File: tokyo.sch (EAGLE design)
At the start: 50 parts, among them J1 254-2X5F, J2 254-2X5M, P1 9774050151, P2 9774050151, P3 9774050151, P4 9774050151, Q1 STD6N95K5, T1 750313823, U1 UCC28710, X1 508-1X3B

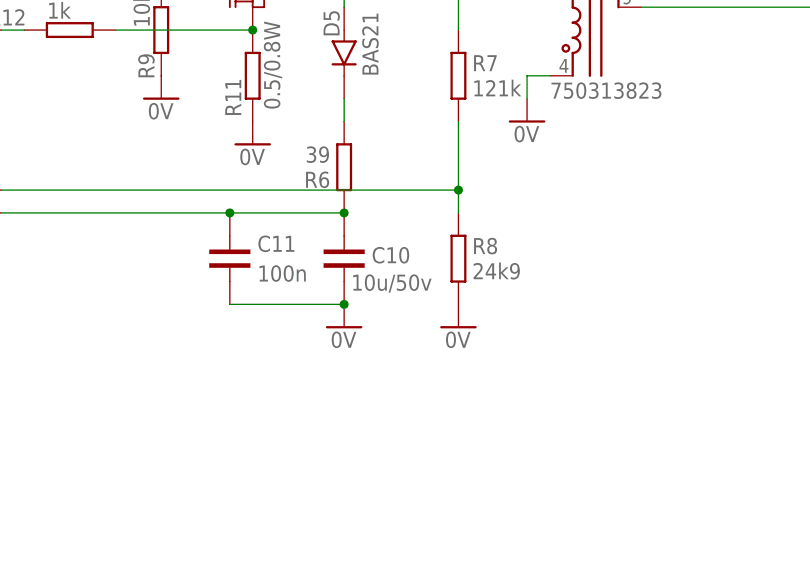
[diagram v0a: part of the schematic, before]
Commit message: Corrected value for C10.
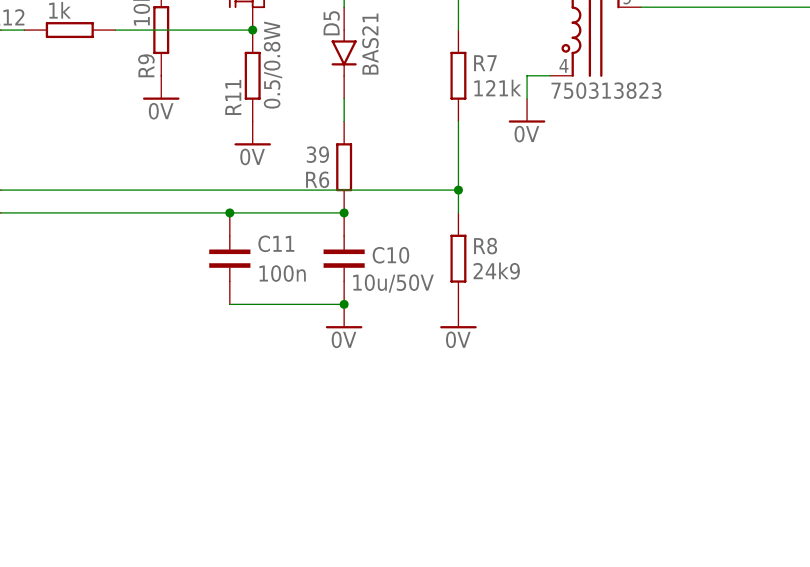
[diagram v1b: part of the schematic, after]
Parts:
- C10: value 10u/50v -> 10u/50V
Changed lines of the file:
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@@
 <part name="U1" library="integratedcircuits" deviceset="UCC28710" device=""/>
 <part name="D5" library="diodes" deviceset="BAS21" device=""/>
-<part name="C10" library="capacitors" deviceset="C" device="1206" value="10u/50v"/>
+<part name="C10" library="capacitors" deviceset="C" device="1206" value="10u/50V"/>
 <part name="R7" library="resistors" deviceset="R" device="0603" value="121k"/>
 <part name="R8" library="resistors" deviceset="R" device="0603" value="24k9"/>

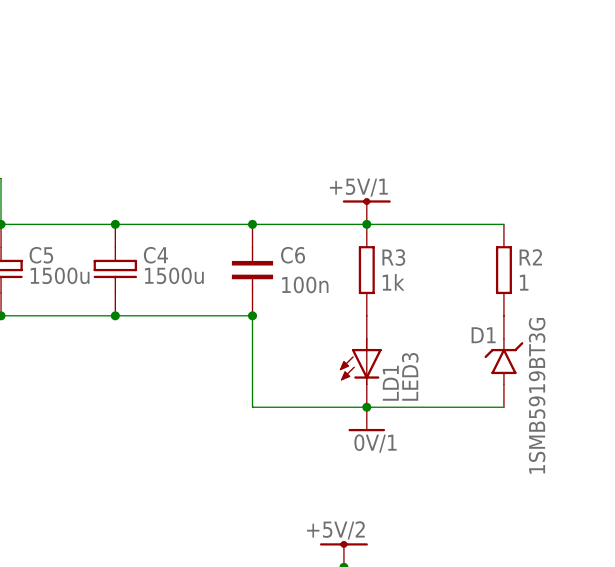
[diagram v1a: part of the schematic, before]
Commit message: Changed R3 to 330 (LD1 was too dim). Corrected BOM (LD1 should be a green LED).
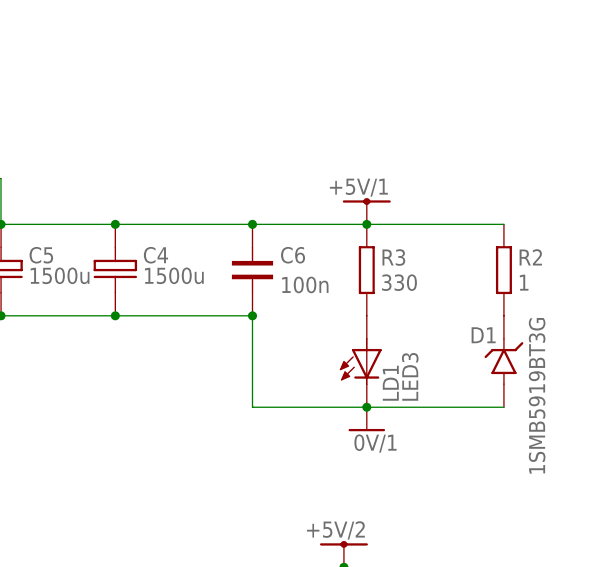
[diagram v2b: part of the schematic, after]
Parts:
- R3: value 1k -> 330
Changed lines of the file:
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@@
 <?xml version="1.0" encoding="utf-8"?>
 <!DOCTYPE eagle SYSTEM "eagle.dtd">
-<eagle version="7.2.0">
+<eagle version="7.3.0">
 <drawing>
 <settings>
@@
 <part name="R11" library="resistors" deviceset="R" device="2512" value="0.5/0.8W"/>
 <part name="C6" library="capacitors" deviceset="C" device="0603" value="100n"/>
-<part name="R3" library="resistors" deviceset="R" device="0603" value="1k"/>
+<part name="R3" library="resistors" deviceset="R" device="0603" value="330"/>
 <part name="R4" library="resistors" deviceset="R" device="1206" value="39"/>
 <part name="LD1" library="unsorted" deviceset="LED3" device=""/>

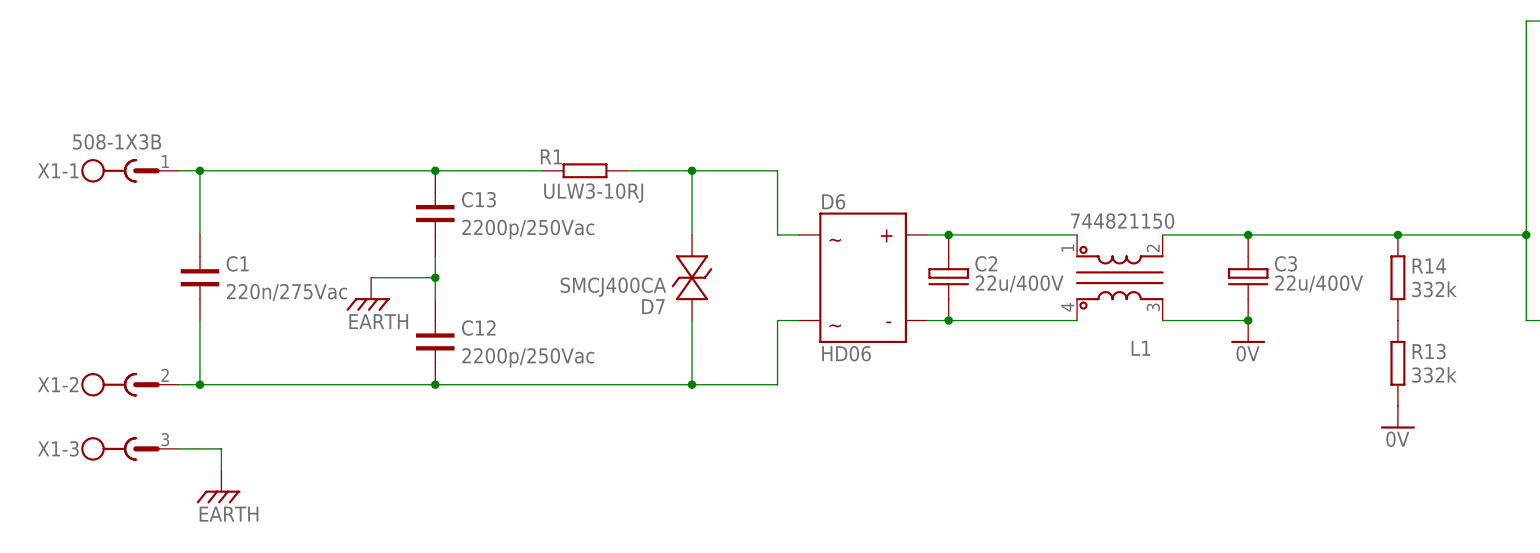
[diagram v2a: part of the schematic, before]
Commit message: Incorporated changes required for EMC tests: replaced transzorb with varistor, changed position of line choke.
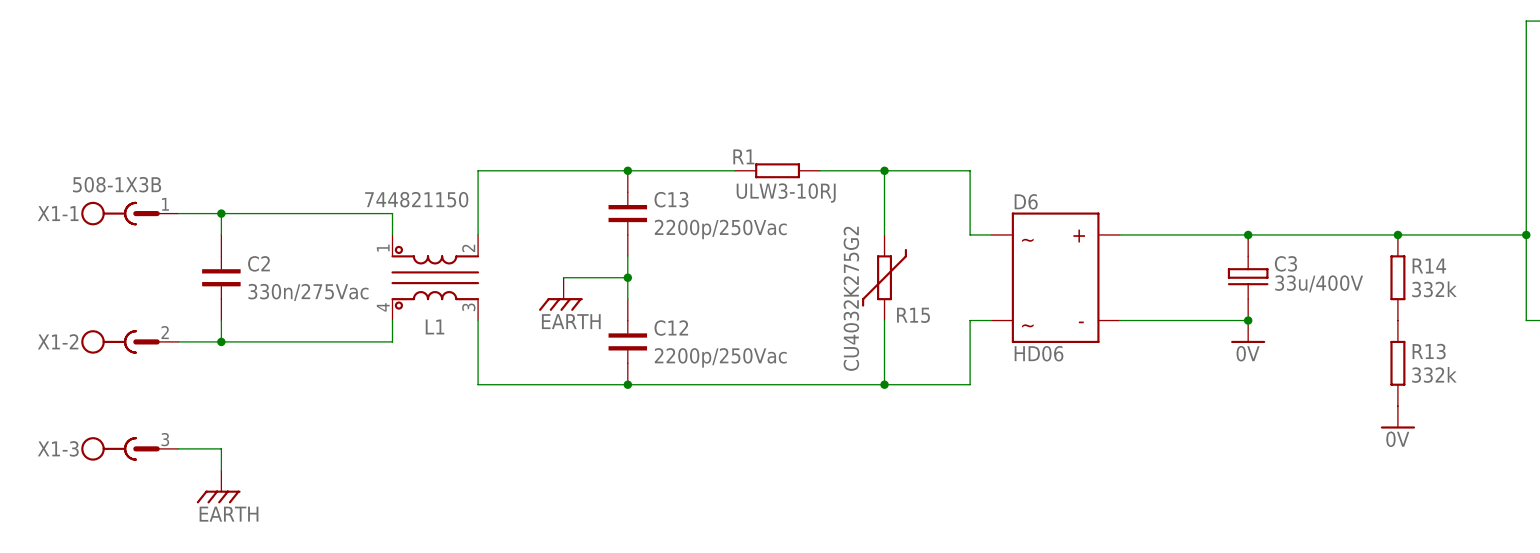
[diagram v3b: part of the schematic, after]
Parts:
- removed C1: 220n/275Vac, capacitors:C14X8
- removed D7: SMCJ400CA, supressors:SMCJ400CA
- added R15: CU4032K275G2, supressors:CU4032K275G2
- C2: value 22u/400V -> 330n/275Vac; device capacitors:C+D13 -> capacitors:C15X8.5
- C3: value 22u/400V -> 33u/400V; device capacitors:C+D13 -> capacitors:C+D18
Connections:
- removed net N$20: C2.2, D6.2, L1.4
- removed net N$21: C2.1, D6.1, L1.1
- new net N$19: C2.1, L1.1, X1-1.1
- new net N$22: C2.2, L1.4, X1-2.1
- net 0V: now also D6.2; no longer L1.3
- net N$1: now also L1.2; no longer C1.1, X1-1.1
- net N$2: now also L1.3, R15.2; no longer C1.2, D7.P$1, X1-2.1
- net N$4: now also R15.1; no longer D7.P$2
- net N$9: now also D6.1; no longer L1.2
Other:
- moved on the sheet: C12, C13, D6, L1, R1, X1-1, X1-2

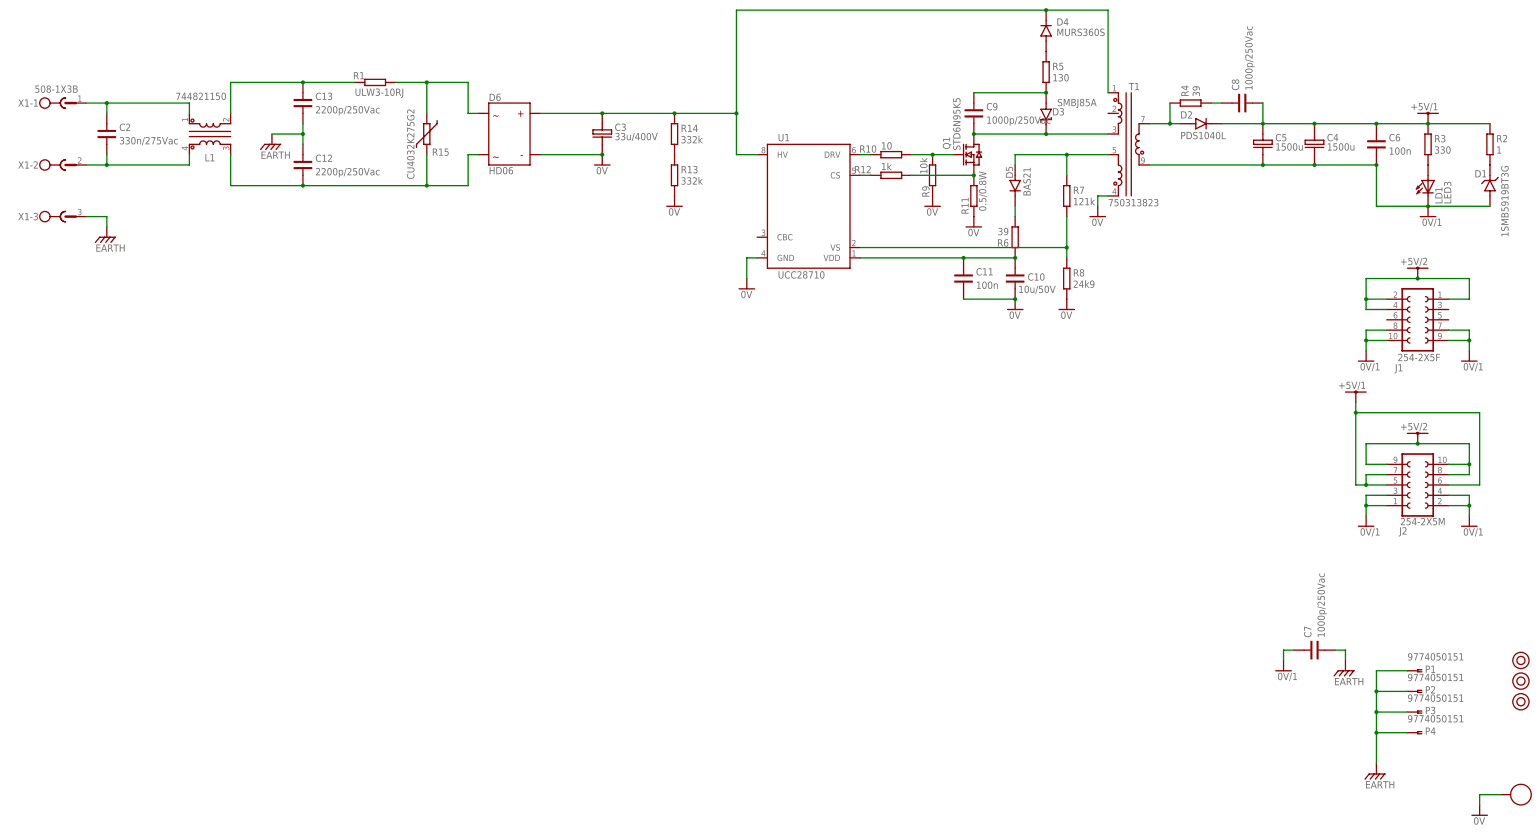
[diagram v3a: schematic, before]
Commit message: Changed R15 to 10 k due to bright LED usage. Renumbered all components.
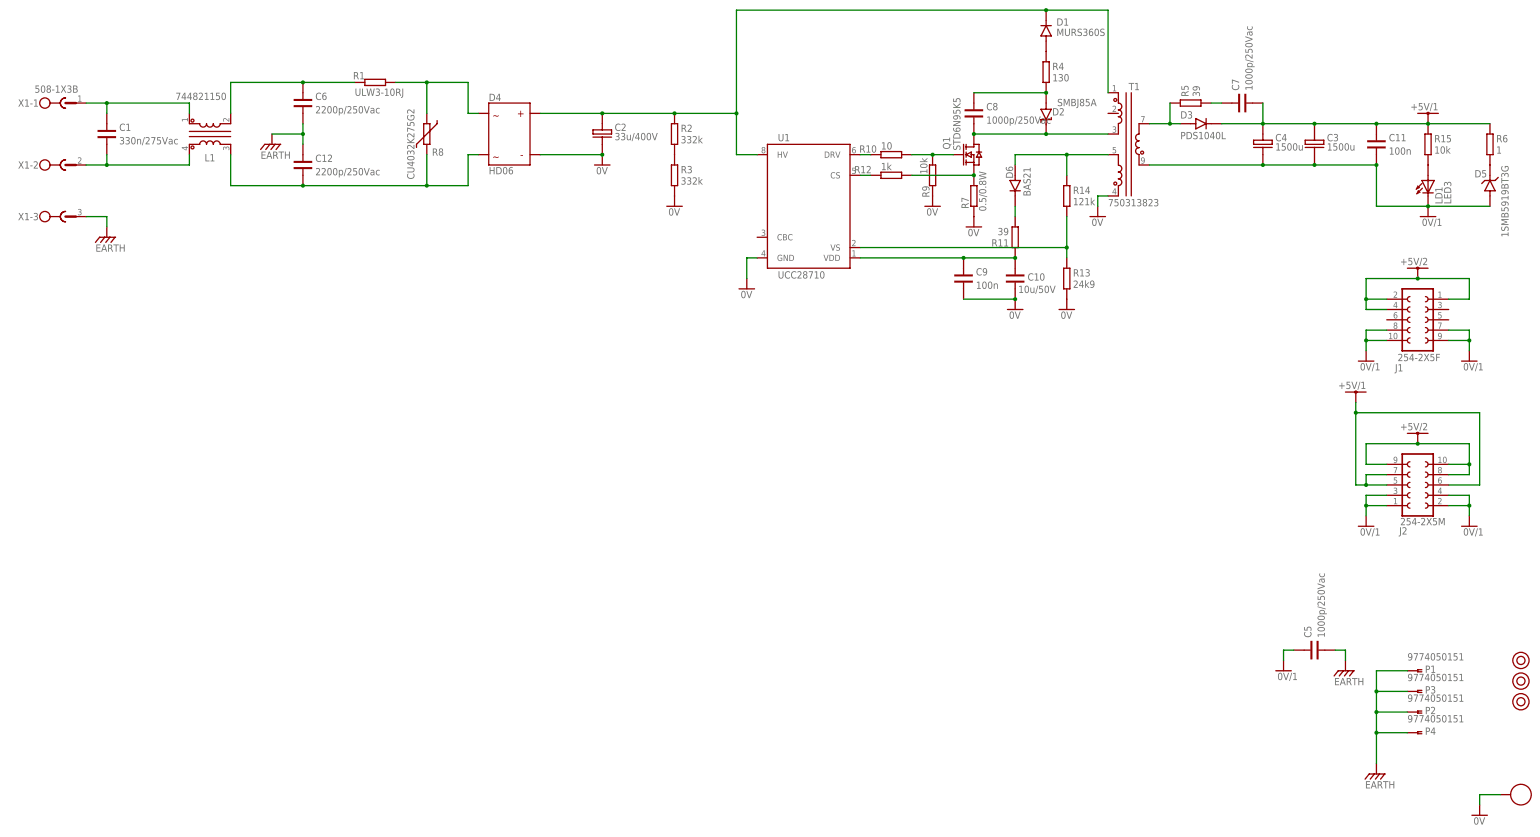
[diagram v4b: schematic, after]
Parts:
- removed C13: 2200p/250Vac, capacitors:C2211
- added C1: 330n/275Vac, capacitors:C15X8.5
- C2: value 330n/275Vac -> 33u/400V; device capacitors:C15X8.5 -> capacitors:C+D18
- C3: value 33u/400V -> 1500u; device capacitors:C+D18 -> capacitors:C+D10
- C5: value 1500u -> 1000p/250Vac; device capacitors:C+D10 -> capacitors:C1812
- C6: value 100n -> 2200p/250Vac; device capacitors:C0603 -> capacitors:C2211
- C9: value 1000p/250Vac -> 100n; device capacitors:C1812 -> capacitors:C0603
- D1: value 1SMB5919BT3G -> MURS360S; device diodes:1SMB5919BT3G -> diodes:MURS360S
- D2: value PDS1040L -> SMBJ85A; device diodes:PDS1040L -> supressors:SMBJ85A
- D3: value SMBJ85A -> PDS1040L; device supressors:SMBJ85A -> diodes:PDS1040L
- D4: value MURS360S -> HD06; device diodes:MURS360S -> diodes:HD06
- D5: value BAS21 -> 1SMB5919BT3G; device diodes:BAS21 -> diodes:1SMB5919BT3G
- D6: value HD06 -> BAS21; device diodes:HD06 -> diodes:BAS21
- R11: value 0.5/0.8W -> 39; device resistors:R2512 -> resistors:R0603
- R13: value 332k -> 24k9; device resistors:R1206 -> resistors:R0603
- R14: value 332k -> 121k; device resistors:R1206 -> resistors:R0603
- R15: value CU4032K275G2 -> 10k; device supressors:CU4032K275G2 -> resistors:R0603
- R2: value 1 -> 332k
- R3: value 330 -> 332k; device resistors:R0603 -> resistors:R1206
- R4: value 39 -> 130
- R5: value 130 -> 39
- R6: value 39 -> 1; device resistors:R0603 -> resistors:R1206
- R7: value 121k -> 0.5/0.8W; device resistors:R0603 -> resistors:R2512
- R8: value 24k9 -> CU4032K275G2; device resistors:R0603 -> supressors:CU4032K275G2
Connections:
- removed net N$16 (its old number): D1.1, R2.2
- new net N$26: D6.1, R11.2
- net +5V/1: now also C11.1, C3.1, C7.2, D3.1, R15.1, R6.1; no longer C5.1, C6.1, C8.2, D2.1, R2.1, R3.1
- net 0V: now also C2.2, C9.2, D4.2, R3.2, R7.1; no longer C11.2, C3.2, D6.2, R11.1, R8.2
- net 0V/1: now also C11.2, C3.2, C5.1, D5.2; no longer C5.2, C6.2, C7.1, D1.2
- net EARTH: now also C5.2, C6.2; no longer C13.2, C7.2
- net N$1: now also C6.1; no longer C13.1
- net N$10: now also D1.2, R4.1; no longer D4.2, R5.1
- net N$11: now also C8.2, D2.C; no longer C9.2, D3.C
- net N$12: now also R7.2; no longer R11.2
- net N$15: now also C9.1, R11.1; no longer C11.1, R6.1
- net N$17: now also C8.1, D2.A, R4.2; no longer C9.1, D3.A, R5.2
- net N$18: now also R13.1, R14.2; no longer R7.2, R8.1
- net N$19: now also C1.1; no longer C2.1
- net N$2: now also D4.4, R8.2; no longer D6.4, R15.2
- net N$22: now also C1.2; no longer C2.2
- net N$3: now also D6.2, R14.1; no longer D5.2, R7.1
- net N$4: now also D4.3, R8.1; no longer D6.3, R15.1
- net N$5: now also R15.2; no longer R3.2
- net N$6: now also C7.1, R5.2; no longer C8.1, R4.2
- net N$7: now also R2.2, R3.1; no longer R13.1, R14.2
- net N$8: now also D3.2, R5.1; no longer D2.2, R4.1
- net N$9: now also C2.1, D1.1, R2.1; no longer C3.1, D6.1, R14.1
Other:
- moved on the sheet: C11, C3, C4, C6, C7, C8, C9, P2, P3, R11, R13, R14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

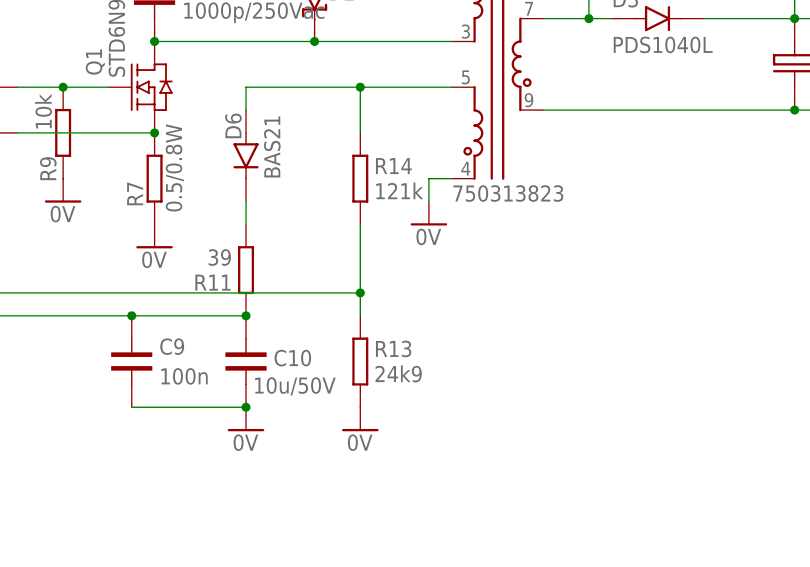
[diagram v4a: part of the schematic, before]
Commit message: Changed values of R13 and R14 in order to get +5.5V on output.
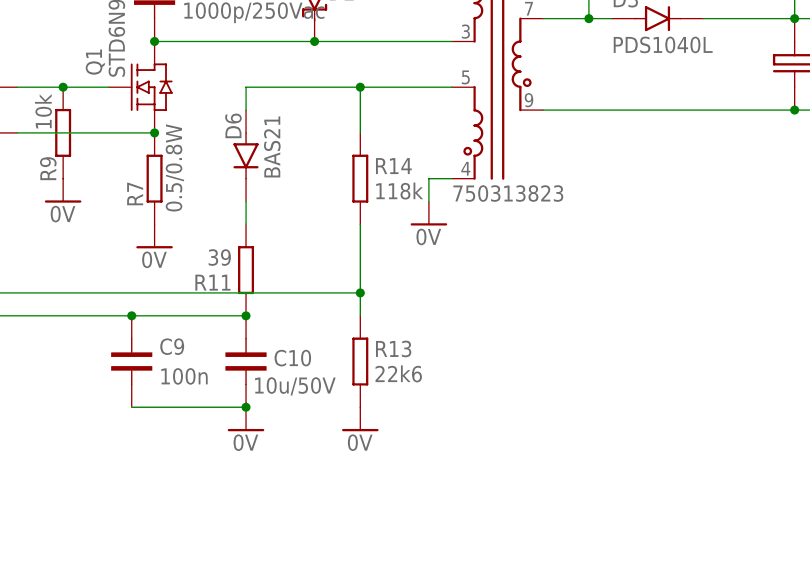
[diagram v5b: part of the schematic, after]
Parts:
- R13: value 24k9 -> 22k6
- R14: value 121k -> 118k
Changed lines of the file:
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@@
 <part name="D6" library="diodes" deviceset="BAS21" device=""/>
 <part name="C10" library="capacitors" deviceset="C" device="1206" value="10u/50V"/>
-<part name="R14" library="resistors" deviceset="R" device="0603" value="121k"/>
-<part name="R13" library="resistors" deviceset="R" device="0603" value="24k9"/>
+<part name="R14" library="resistors" deviceset="R" device="0603" value="118k"/>
+<part name="R13" library="resistors" deviceset="R" device="0603" value="22k6"/>
 <part name="R12" library="resistors" deviceset="R" device="0603" value="1k"/>
 <part name="R7" library="resistors" deviceset="R" device="2512" value="0.5/0.8W"/>
